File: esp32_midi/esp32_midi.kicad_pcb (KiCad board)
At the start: 2 copper layers, 2 parts, among them U1 ESP32-S3-WROOM-2, U2 AMS1117-3.3

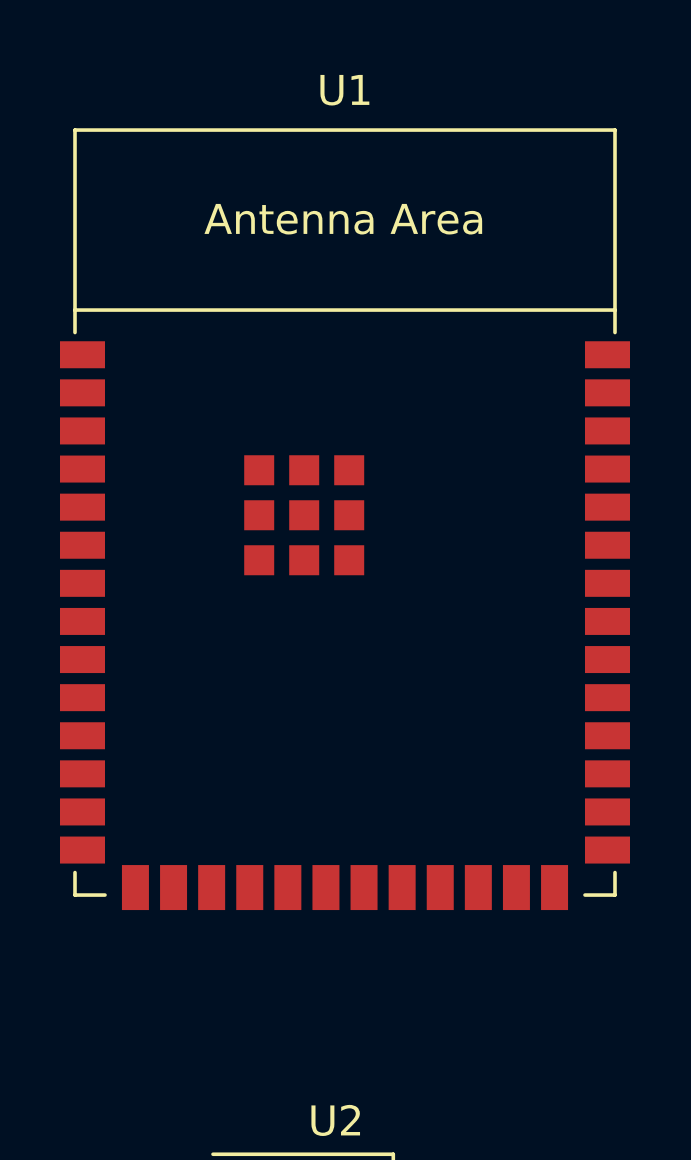
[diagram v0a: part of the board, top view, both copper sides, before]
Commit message: More footprints applied
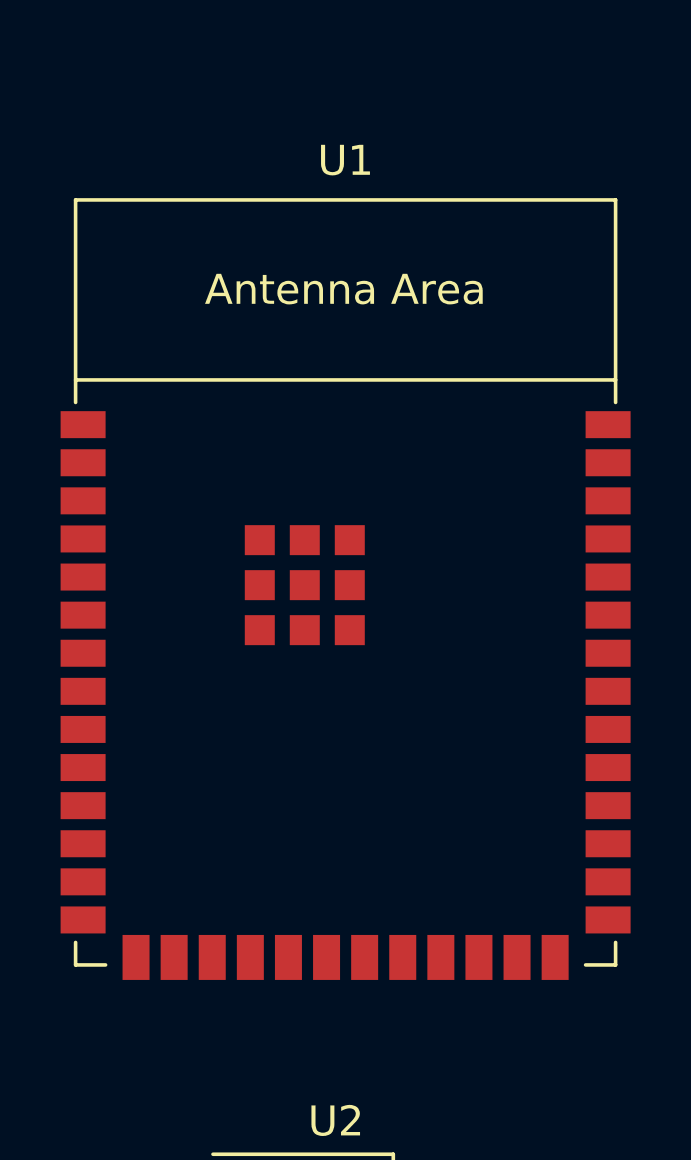
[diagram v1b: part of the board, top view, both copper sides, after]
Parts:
- moved U1 2.33 mm to (111.6, 50.1)

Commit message: Add ordentliche-teile
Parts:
- removed U1: ESP32-S3-WROOM-2, Espressif:ESP32-S3-WROOM-2
- removed U2: AMS1117-3.3, Package_TO_SOT_SMD:SOT-223-3_TabPin2

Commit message: Started work on PCB
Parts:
- added C1: 100n, Capacitor_SMD:C_0402_1005Metric, F.Cu at (380.5, 28.0)
- added C10: 10u, Capacitor_SMD:C_0603_1608Metric, F.Cu at (390.2, 109.4)
- added C2: 100n, Capacitor_SMD:C_0402_1005Metric, F.Cu at (380.5, 30.0)
- added C3: 100n, Capacitor_SMD:C_0402_1005Metric, F.Cu at (380.5, 31.9)
- added C4: 680µF, Capacitor_SMD:CP_Elec_10x10, F.Cu at (368.4, 69.8)
- added C5: 220µF, Capacitor_SMD:CP_Elec_10x10, F.Cu at (368.4, 81.7)
- added C6: 100n, Capacitor_SMD:C_0402_1005Metric, F.Cu at (380.5, 33.9)
- added C7: 100n, Capacitor_SMD:C_0402_1005Metric, F.Cu at (389.7, 111.6)
- added C8: 1u, Capacitor_SMD:C_0603_1608Metric, F.Cu at (390.2, 106.9)
- added C9: 100n, Capacitor_SMD:C_0402_1005Metric, F.Cu at (389.7, 113.6)
- added D1: D, Diode_SMD:D_SOD-123, F.Cu at (344.4, 14.4)
- added D10: WS2812B, LED_SMD:LED_WS2812B_PLCC4_5.0x5.0mm_P3.2mm, F.Cu at (185.6, 74.3)
- added D11: WS2812B, LED_SMD:LED_WS2812B_PLCC4_5.0x5.0mm_P3.2mm, F.Cu at (207.1, 74.3)
- added D12: WS2812B, LED_SMD:LED_WS2812B_PLCC4_5.0x5.0mm_P3.2mm, F.Cu at (228.6, 74.3)
- added D13: WS2812B, LED_SMD:LED_WS2812B_PLCC4_5.0x5.0mm_P3.2mm, F.Cu at (250.1, 74.3)
- added D14: WS2812B, LED_SMD:LED_WS2812B_PLCC4_5.0x5.0mm_P3.2mm, F.Cu at (271.6, 74.3)
- added D15: WS2812B, LED_SMD:LED_WS2812B_PLCC4_5.0x5.0mm_P3.2mm, F.Cu at (293.1, 74.3)
- added D16: WS2812B, LED_SMD:LED_WS2812B_PLCC4_5.0x5.0mm_P3.2mm, F.Cu at (314.6, 74.3)
- added D17: WS2812B, LED_SMD:LED_WS2812B_PLCC4_5.0x5.0mm_P3.2mm, F.Cu at (336.1, 74.3)
- added D18: WS2812B, LED_SMD:LED_WS2812B_PLCC4_5.0x5.0mm_P3.2mm, F.Cu at (185.6, 95.8)
- added D19: WS2812B, LED_SMD:LED_WS2812B_PLCC4_5.0x5.0mm_P3.2mm, F.Cu at (207.1, 95.8)
- added D2: D, Diode_SMD:D_SOD-123, F.Cu at (344.4, 17.8)
- added D20: WS2812B, LED_SMD:LED_WS2812B_PLCC4_5.0x5.0mm_P3.2mm, F.Cu at (228.6, 95.8)
- added D21: WS2812B, LED_SMD:LED_WS2812B_PLCC4_5.0x5.0mm_P3.2mm, F.Cu at (250.1, 95.8)
- added D22: WS2812B, LED_SMD:LED_WS2812B_PLCC4_5.0x5.0mm_P3.2mm, F.Cu at (271.6, 95.8)
- added D23: WS2812B, LED_SMD:LED_WS2812B_PLCC4_5.0x5.0mm_P3.2mm, F.Cu at (293.1, 95.8)
- added D24: WS2812B, LED_SMD:LED_WS2812B_PLCC4_5.0x5.0mm_P3.2mm, F.Cu at (314.6, 95.8)
- added D25: WS2812B, LED_SMD:LED_WS2812B_PLCC4_5.0x5.0mm_P3.2mm, F.Cu at (336.1, 95.8)
- added D26: WS2812B, LED_SMD:LED_WS2812B_PLCC4_5.0x5.0mm_P3.2mm, F.Cu at (185.6, 117.3)
- added D27: WS2812B, LED_SMD:LED_WS2812B_PLCC4_5.0x5.0mm_P3.2mm, F.Cu at (207.1, 117.3)
- added D28: WS2812B, LED_SMD:LED_WS2812B_PLCC4_5.0x5.0mm_P3.2mm, F.Cu at (228.6, 117.3)
- added D29: WS2812B, LED_SMD:LED_WS2812B_PLCC4_5.0x5.0mm_P3.2mm, F.Cu at (250.1, 117.3)
- added D3: D, Diode_SMD:D_SOD-123, F.Cu at (344.4, 21.1)
- added D30: WS2812B, LED_SMD:LED_WS2812B_PLCC4_5.0x5.0mm_P3.2mm, F.Cu at (271.6, 117.3)
- added D31: WS2812B, LED_SMD:LED_WS2812B_PLCC4_5.0x5.0mm_P3.2mm, F.Cu at (293.1, 117.3)
- added D32: WS2812B, LED_SMD:LED_WS2812B_PLCC4_5.0x5.0mm_P3.2mm, F.Cu at (314.6, 117.3)
- added D33: WS2812B, LED_SMD:LED_WS2812B_PLCC4_5.0x5.0mm_P3.2mm, F.Cu at (336.1, 117.3)
- added D34: WS2812B, LED_SMD:LED_WS2812B_PLCC4_5.0x5.0mm_P3.2mm, F.Cu at (185.6, 138.8)
- added D35: WS2812B, LED_SMD:LED_WS2812B_PLCC4_5.0x5.0mm_P3.2mm, F.Cu at (207.1, 138.8)
- added D36: WS2812B, LED_SMD:LED_WS2812B_PLCC4_5.0x5.0mm_P3.2mm, F.Cu at (228.6, 138.8)
- added D37: WS2812B, LED_SMD:LED_WS2812B_PLCC4_5.0x5.0mm_P3.2mm, F.Cu at (250.1, 138.8)
- added D38: WS2812B, LED_SMD:LED_WS2812B_PLCC4_5.0x5.0mm_P3.2mm, F.Cu at (271.6, 138.8)
- added D39: WS2812B, LED_SMD:LED_WS2812B_PLCC4_5.0x5.0mm_P3.2mm, F.Cu at (293.1, 138.8)
- added D4: D, Diode_SMD:D_SOD-123, F.Cu at (344.4, 24.5)
- added D40: WS2812B, LED_SMD:LED_WS2812B_PLCC4_5.0x5.0mm_P3.2mm, F.Cu at (314.6, 138.8)
- added D41: WS2812B, LED_SMD:LED_WS2812B_PLCC4_5.0x5.0mm_P3.2mm, F.Cu at (336.1, 138.8)
- added D42: WS2812B, LED_SMD:LED_WS2812B_PLCC4_5.0x5.0mm_P3.2mm, F.Cu at (185.6, 160.3)
- added D43: WS2812B, LED_SMD:LED_WS2812B_PLCC4_5.0x5.0mm_P3.2mm, F.Cu at (207.1, 160.3)
- added D44: WS2812B, LED_SMD:LED_WS2812B_PLCC4_5.0x5.0mm_P3.2mm, F.Cu at (228.6, 160.3)
- added D45: WS2812B, LED_SMD:LED_WS2812B_PLCC4_5.0x5.0mm_P3.2mm, F.Cu at (250.1, 160.3)
- added D46: WS2812B, LED_SMD:LED_WS2812B_PLCC4_5.0x5.0mm_P3.2mm, F.Cu at (271.6, 160.3)
- added D47: WS2812B, LED_SMD:LED_WS2812B_PLCC4_5.0x5.0mm_P3.2mm, F.Cu at (293.1, 160.3)
- added D48: WS2812B, LED_SMD:LED_WS2812B_PLCC4_5.0x5.0mm_P3.2mm, F.Cu at (314.6, 160.3)
- added D49: WS2812B, LED_SMD:LED_WS2812B_PLCC4_5.0x5.0mm_P3.2mm, F.Cu at (336.1, 160.3)
- added D5: 1N4148, Diode_SMD:D_SOD-123, F.Cu at (235.5, 38.5)
- added D50: WS2812B, LED_SMD:LED_WS2812B_PLCC4_5.0x5.0mm_P3.2mm, F.Cu at (185.6, 181.8)
- added D51: WS2812B, LED_SMD:LED_WS2812B_PLCC4_5.0x5.0mm_P3.2mm, F.Cu at (207.1, 181.8)
- added D52: WS2812B, LED_SMD:LED_WS2812B_PLCC4_5.0x5.0mm_P3.2mm, F.Cu at (228.6, 181.8)
- added D53: WS2812B, LED_SMD:LED_WS2812B_PLCC4_5.0x5.0mm_P3.2mm, F.Cu at (250.1, 181.8)
- added D54: WS2812B, LED_SMD:LED_WS2812B_PLCC4_5.0x5.0mm_P3.2mm, F.Cu at (271.6, 181.8)
- added D55: WS2812B, LED_SMD:LED_WS2812B_PLCC4_5.0x5.0mm_P3.2mm, F.Cu at (293.1, 181.8)
- added D56: WS2812B, LED_SMD:LED_WS2812B_PLCC4_5.0x5.0mm_P3.2mm, F.Cu at (314.6, 181.8)
- added D57: WS2812B, LED_SMD:LED_WS2812B_PLCC4_5.0x5.0mm_P3.2mm, F.Cu at (336.1, 181.8)
- added D58: WS2812B, LED_SMD:LED_WS2812B_PLCC4_5.0x5.0mm_P3.2mm, F.Cu at (185.6, 203.3)
- added D59: WS2812B, LED_SMD:LED_WS2812B_PLCC4_5.0x5.0mm_P3.2mm, F.Cu at (207.1, 203.3)
- added D6: LED, LED_SMD:LED_0603_1608Metric, F.Cu at (386.2, 106.9)
- added D60: WS2812B, LED_SMD:LED_WS2812B_PLCC4_5.0x5.0mm_P3.2mm, F.Cu at (228.6, 203.3)
- added D61: WS2812B, LED_SMD:LED_WS2812B_PLCC4_5.0x5.0mm_P3.2mm, F.Cu at (250.1, 203.3)
- added D62: WS2812B, LED_SMD:LED_WS2812B_PLCC4_5.0x5.0mm_P3.2mm, F.Cu at (271.6, 203.3)
- added D63: WS2812B, LED_SMD:LED_WS2812B_PLCC4_5.0x5.0mm_P3.2mm, F.Cu at (293.1, 203.3)
- added D64: WS2812B, LED_SMD:LED_WS2812B_PLCC4_5.0x5.0mm_P3.2mm, F.Cu at (314.6, 203.3)
- added D65: WS2812B, LED_SMD:LED_WS2812B_PLCC4_5.0x5.0mm_P3.2mm, F.Cu at (336.1, 203.3)
- added D66: WS2812B, LED_SMD:LED_WS2812B_PLCC4_5.0x5.0mm_P3.2mm, F.Cu at (185.6, 224.8)
- added D67: WS2812B, LED_SMD:LED_WS2812B_PLCC4_5.0x5.0mm_P3.2mm, F.Cu at (207.1, 224.8)
- added D68: WS2812B, LED_SMD:LED_WS2812B_PLCC4_5.0x5.0mm_P3.2mm, F.Cu at (228.6, 224.8)
- added D69: WS2812B, LED_SMD:LED_WS2812B_PLCC4_5.0x5.0mm_P3.2mm, F.Cu at (250.1, 224.8)
- added D7: LED, LED_SMD:LED_0603_1608Metric, F.Cu at (386.2, 109.5)
- added D70: WS2812B, LED_SMD:LED_WS2812B_PLCC4_5.0x5.0mm_P3.2mm, F.Cu at (271.6, 224.8)
- added D71: WS2812B, LED_SMD:LED_WS2812B_PLCC4_5.0x5.0mm_P3.2mm, F.Cu at (293.1, 224.8)
- added D72: WS2812B, LED_SMD:LED_WS2812B_PLCC4_5.0x5.0mm_P3.2mm, F.Cu at (314.6, 224.8)
- added D73: WS2812B, LED_SMD:LED_WS2812B_PLCC4_5.0x5.0mm_P3.2mm, F.Cu at (336.1, 224.8)
- added D74: WS2812B, LED_SMD:LED_WS2812B_PLCC4_5.0x5.0mm_P3.2mm, F.Cu at (185.6, 246.3)
- added D75: WS2812B, LED_SMD:LED_WS2812B_PLCC4_5.0x5.0mm_P3.2mm, F.Cu at (207.1, 246.3)
- added D76: WS2812B, LED_SMD:LED_WS2812B_PLCC4_5.0x5.0mm_P3.2mm, F.Cu at (228.6, 246.3)
- added D77: WS2812B, LED_SMD:LED_WS2812B_PLCC4_5.0x5.0mm_P3.2mm, F.Cu at (250.1, 246.3)
- added D78: WS2812B, LED_SMD:LED_WS2812B_PLCC4_5.0x5.0mm_P3.2mm, F.Cu at (271.6, 246.3)
- added D79: WS2812B, LED_SMD:LED_WS2812B_PLCC4_5.0x5.0mm_P3.2mm, F.Cu at (293.1, 246.3)
- added D8: LED, LED_SMD:LED_0603_1608Metric, F.Cu at (386.2, 112.1)
- added D80: WS2812B, LED_SMD:LED_WS2812B_PLCC4_5.0x5.0mm_P3.2mm, F.Cu at (314.6, 246.3)
- added D81: WS2812B, LED_SMD:LED_WS2812B_PLCC4_5.0x5.0mm_P3.2mm, F.Cu at (336.1, 246.3)
- added D82: SS54, Diode_SMD:D_SMA, F.Cu at (365.1, 89.9)
- added D9: LED5V, LED_SMD:LED_0603_1608Metric, F.Cu at (386.2, 114.7)
- added J1: Conn_Display, Connector_PinHeader_2.54mm:PinHeader_1x08_P2.54mm_Vertical, F.Cu at (222.5, 59.0)
- added J2: 5V-12V, Connector_BarrelJack:BarrelJack_Wuerth_6941xx301002, F.Cu at (307.6, 25.4)
- added J4: MIDI 1 OUT, ordentliche-teile:scheißmidi, F.Cu at (260.8, 11.5)
- added J5: MIDI 1 IN, ordentliche-teile:scheißmidi, F.Cu at (238.1, 11.7)
- added J6: MIDI 1 OUT, ordentliche-teile:scheißmidi, F.Cu at (215.0, 11.5)
- added L1: 33µH, Inductor_SMD:L_10.4x10.4_H4.8, F.Cu at (381.4, 82.2)
- added Q1: BSS138, Package_TO_SOT_SMD:SOT-23, F.Cu at (264.0, 32.0)
- added Q2: SS8050_C2150, Package_TO_SOT_SMD:TSOT-23, F.Cu at (401.1, 96.4)
- added Q3: SS8050_C2150, Package_TO_SOT_SMD:TSOT-23, F.Cu at (401.1, 100.8)
- added Q4: BSS138, Package_TO_SOT_SMD:SOT-23, F.Cu at (218.5, 30.6)
- added R1: 10k, Resistor_SMD:R_0402_1005Metric, F.Cu at (380.5, 35.9)
- added R10: 10k, Resistor_SMD:R_0402_1005Metric, F.Cu at (397.0, 95.2)
- added R11: 1k, Resistor_SMD:R_0402_1005Metric, F.Cu at (397.0, 97.1)
- added R12: 1k, Resistor_SMD:R_0402_1005Metric, F.Cu at (397.0, 99.1)
- added R13: 1k, Resistor_SMD:R_0402_1005Metric, F.Cu at (397.0, 101.1)
- added R14: 1k, Resistor_SMD:R_0402_1005Metric, F.Cu at (397.0, 103.1)
- added R15: 220, Resistor_SMD:R_0402_1005Metric, F.Cu at (210.0, 31.0)
- added R16: R_Variable, ordentliche-teile:scheißfader, B.Cu at (185.4, 324.0)
- added R17: R_Variable, ordentliche-teile:scheißfader, B.Cu at (206.9, 324.0)
- added R18: R_Variable, ordentliche-teile:scheißfader, B.Cu at (228.4, 324.0)
- added R19: R_Variable, ordentliche-teile:scheißfader, B.Cu at (249.9, 324.0)
- added R2: 220, Resistor_SMD:R_0402_1005Metric, F.Cu at (256.0, 30.0)
- added R20: R_Variable, ordentliche-teile:scheißfader, B.Cu at (271.4, 324.0)
- added R21: R_Variable, ordentliche-teile:scheißfader, B.Cu at (292.9, 324.0)
- added R22: R_Variable, ordentliche-teile:scheißfader, B.Cu at (314.4, 324.0)
- added R23: R_Variable, ordentliche-teile:scheißfader, B.Cu at (335.9, 324.0)
- added R24: R_Variable, Potentiometer_THT:Potentiometer_Alps_RK09L_Single_Vertical, F.Cu at (184.5, 262.5)
- added R25: R_Variable, Potentiometer_THT:Potentiometer_Alps_RK09L_Single_Vertical, F.Cu at (206.0, 262.5)
- added R26: R_Variable, Potentiometer_THT:Potentiometer_Alps_RK09L_Single_Vertical, F.Cu at (227.5, 262.5)
- added R27: R_Variable, Potentiometer_THT:Potentiometer_Alps_RK09L_Single_Vertical, F.Cu at (249.0, 262.5)
- added R28: R_Variable, Potentiometer_THT:Potentiometer_Alps_RK09L_Single_Vertical, F.Cu at (270.5, 262.5)
- added R29: R_Variable, Potentiometer_THT:Potentiometer_Alps_RK09L_Single_Vertical, F.Cu at (292.0, 262.5)
- added R3: 220, Resistor_SMD:R_0402_1005Metric, F.Cu at (241.0, 44.5)
- added R30: R_Variable, Potentiometer_THT:Potentiometer_Alps_RK09L_Single_Vertical, F.Cu at (313.5, 262.5)
- added R31: R_Variable, Potentiometer_THT:Potentiometer_Alps_RK09L_Single_Vertical, F.Cu at (335.0, 262.5)
- added R32: R_Variable, Potentiometer_THT:Potentiometer_Alps_RK09L_Single_Vertical, F.Cu at (184.5, 284.0)
- added R33: R_Variable, Potentiometer_THT:Potentiometer_Alps_RK09L_Single_Vertical, F.Cu at (206.0, 284.0)
- added R34: R_Variable, Potentiometer_THT:Potentiometer_Alps_RK09L_Single_Vertical, F.Cu at (227.5, 284.0)
- added R35: R_Variable, Potentiometer_THT:Potentiometer_Alps_RK09L_Single_Vertical, F.Cu at (249.0, 284.0)
- added R36: R_Variable, Potentiometer_THT:Potentiometer_Alps_RK09L_Single_Vertical, F.Cu at (270.5, 284.0)
- added R37: R_Variable, Potentiometer_THT:Potentiometer_Alps_RK09L_Single_Vertical, F.Cu at (292.0, 284.0)
- added R38: R_Variable, Potentiometer_THT:Potentiometer_Alps_RK09L_Single_Vertical, F.Cu at (313.5, 284.0)
- added R39: R_Variable, Potentiometer_THT:Potentiometer_Alps_RK09L_Single_Vertical, F.Cu at (335.0, 284.0)
- added R4: 220, Resistor_SMD:R_0402_1005Metric, F.Cu at (233.0, 33.0)
- added R40: R_Variable, Potentiometer_THT:Potentiometer_Alps_RK09L_Single_Vertical, F.Cu at (184.5, 305.5)
- added R41: R_Variable, Potentiometer_THT:Potentiometer_Alps_RK09L_Single_Vertical, F.Cu at (206.0, 305.5)
- added R42: R_Variable, Potentiometer_THT:Potentiometer_Alps_RK09L_Single_Vertical, F.Cu at (227.5, 305.5)
- added R43: R_Variable, Potentiometer_THT:Potentiometer_Alps_RK09L_Single_Vertical, F.Cu at (249.0, 305.5)
- added R44: R_Variable, Potentiometer_THT:Potentiometer_Alps_RK09L_Single_Vertical, F.Cu at (270.5, 305.5)
- added R45: R_Variable, Potentiometer_THT:Potentiometer_Alps_RK09L_Single_Vertical, F.Cu at (292.0, 305.5)
- added R46: R_Variable, Potentiometer_THT:Potentiometer_Alps_RK09L_Single_Vertical, F.Cu at (313.5, 305.5)
- added R47: R_Variable, Potentiometer_THT:Potentiometer_Alps_RK09L_Single_Vertical, F.Cu at (335.0, 305.5)
- added R48: 10k, Resistor_SMD:R_0402_1005Metric, F.Cu at (472.0, 175.0)
- added R49: 10k, Resistor_SMD:R_0402_1005Metric, F.Cu at (472.5, 180.5)
- added R5: 12k, Resistor_SMD:R_0402_1005Metric, F.Cu at (394.1, 95.2)
- added R50: 10k, Resistor_SMD:R_0402_1005Metric, F.Cu at (479.1, 194.9)
- added R51: 5k1, Resistor_SMD:R_0402_1005Metric, F.Cu at (380.5, 37.9)
- added R52: 5k1, Resistor_SMD:R_0402_1005Metric, F.Cu at (380.5, 39.9)
- added R6: 12k, Resistor_SMD:R_0402_1005Metric, F.Cu at (394.1, 97.1)
- added R7: 5k1, Resistor_SMD:R_0402_1005Metric, F.Cu at (394.1, 99.1)
- added R8: 5k1, Resistor_SMD:R_0402_1005Metric, F.Cu at (394.1, 101.1)
- added R9: 10k, Resistor_SMD:R_0402_1005Metric, F.Cu at (394.1, 103.1)
- added SW1: SW_SPST, Button_Switch_THT:SW_PUSH_6mm_H13mm, F.Cu at (179.8, 22.2)
- added SW10: SW_SPST, ordentliche-teile:scheißbutton, F.Cu at (178.5, 102.0)
- added SW11: SW_SPST, ordentliche-teile:scheißbutton, F.Cu at (200.0, 102.0)
- added SW12: SW_SPST, ordentliche-teile:scheißbutton, F.Cu at (221.5, 102.0)
- added SW13: SW_SPST, ordentliche-teile:scheißbutton, F.Cu at (243.0, 102.0)
- added SW14: SW_SPST, ordentliche-teile:scheißbutton, F.Cu at (264.5, 102.0)
- added SW15: SW_SPST, ordentliche-teile:scheißbutton, F.Cu at (286.0, 102.0)
- added SW16: SW_SPST, ordentliche-teile:scheißbutton, F.Cu at (307.5, 102.0)
- added SW17: SW_SPST, ordentliche-teile:scheißbutton, F.Cu at (329.0, 102.0)
- added SW18: SW_SPST, ordentliche-teile:scheißbutton, F.Cu at (178.5, 123.5)
- added SW19: SW_SPST, ordentliche-teile:scheißbutton, F.Cu at (200.0, 123.5)
- added SW2: SW_SPST, ordentliche-teile:scheißbutton, F.Cu at (178.5, 80.5)
- added SW20: SW_SPST, ordentliche-teile:scheißbutton, F.Cu at (221.5, 123.5)
- added SW21: SW_SPST, ordentliche-teile:scheißbutton, F.Cu at (243.0, 123.5)
- added SW22: SW_SPST, ordentliche-teile:scheißbutton, F.Cu at (264.5, 123.5)
- added SW23: SW_SPST, ordentliche-teile:scheißbutton, F.Cu at (286.0, 123.5)
- added SW24: SW_SPST, ordentliche-teile:scheißbutton, F.Cu at (307.5, 123.5)
- added SW25: SW_SPST, ordentliche-teile:scheißbutton, F.Cu at (329.0, 123.5)
- added SW26: SW_SPST, ordentliche-teile:scheißbutton, F.Cu at (178.5, 145.0)
- added SW27: SW_SPST, ordentliche-teile:scheißbutton, F.Cu at (200.0, 145.0)
- added SW28: SW_SPST, ordentliche-teile:scheißbutton, F.Cu at (221.5, 145.0)
- added SW29: SW_SPST, ordentliche-teile:scheißbutton, F.Cu at (243.0, 145.0)
- added SW3: SW_SPST, ordentliche-teile:scheißbutton, F.Cu at (200.0, 80.5)
- added SW30: SW_SPST, ordentliche-teile:scheißbutton, F.Cu at (264.5, 145.0)
- added SW31: SW_SPST, ordentliche-teile:scheißbutton, F.Cu at (286.0, 145.0)
- added SW32: SW_SPST, ordentliche-teile:scheißbutton, F.Cu at (307.5, 145.0)
- added SW33: SW_SPST, ordentliche-teile:scheißbutton, F.Cu at (329.0, 145.0)
- added SW34: SW_SPST, ordentliche-teile:scheißbutton, F.Cu at (178.5, 166.5)
- added SW35: SW_SPST, ordentliche-teile:scheißbutton, F.Cu at (200.0, 166.5)
- added SW36: SW_SPST, ordentliche-teile:scheißbutton, F.Cu at (221.5, 166.5)
- added SW37: SW_SPST, ordentliche-teile:scheißbutton, F.Cu at (243.0, 166.5)
- added SW38: SW_SPST, ordentliche-teile:scheißbutton, F.Cu at (264.5, 166.5)
- added SW39: SW_SPST, ordentliche-teile:scheißbutton, F.Cu at (286.0, 166.5)
- added SW4: SW_SPST, ordentliche-teile:scheißbutton, F.Cu at (221.5, 80.5)
- added SW40: SW_SPST, ordentliche-teile:scheißbutton, F.Cu at (307.5, 166.5)
- added SW41: SW_SPST, ordentliche-teile:scheißbutton, F.Cu at (329.0, 166.5)
- added SW42: SW_SPST, ordentliche-teile:scheißbutton, F.Cu at (178.5, 188.0)
- added SW43: SW_SPST, ordentliche-teile:scheißbutton, F.Cu at (200.0, 188.0)
- added SW44: SW_SPST, ordentliche-teile:scheißbutton, F.Cu at (221.5, 188.0)
- added SW45: SW_SPST, ordentliche-teile:scheißbutton, F.Cu at (243.0, 188.0)
- added SW46: SW_SPST, ordentliche-teile:scheißbutton, F.Cu at (264.5, 188.0)
- added SW47: SW_SPST, ordentliche-teile:scheißbutton, F.Cu at (286.0, 188.0)
- added SW48: SW_SPST, ordentliche-teile:scheißbutton, F.Cu at (307.5, 188.0)
- added SW49: SW_SPST, ordentliche-teile:scheißbutton, F.Cu at (329.0, 188.0)
- added SW5: SW_SPST, ordentliche-teile:scheißbutton, F.Cu at (243.0, 80.5)
- added SW50: SW_SPST, ordentliche-teile:scheißbutton, F.Cu at (178.5, 209.5)
- added SW51: SW_SPST, ordentliche-teile:scheißbutton, F.Cu at (200.0, 209.5)
- added SW52: SW_SPST, ordentliche-teile:scheißbutton, F.Cu at (221.5, 209.5)
- added SW53: SW_SPST, ordentliche-teile:scheißbutton, F.Cu at (243.0, 209.5)
- added SW54: SW_SPST, ordentliche-teile:scheißbutton, F.Cu at (264.5, 209.5)
- added SW55: SW_SPST, ordentliche-teile:scheißbutton, F.Cu at (286.0, 209.5)
- added SW56: SW_SPST, ordentliche-teile:scheißbutton, F.Cu at (307.5, 209.5)
- added SW57: SW_SPST, ordentliche-teile:scheißbutton, F.Cu at (329.0, 209.5)
- added SW58: SW_SPST, ordentliche-teile:scheißbutton, F.Cu at (178.5, 231.0)
- added SW59: SW_SPST, ordentliche-teile:scheißbutton, F.Cu at (200.0, 231.0)
- added SW6: SW_SPST, ordentliche-teile:scheißbutton, F.Cu at (264.5, 80.5)
- added SW60: SW_SPST, ordentliche-teile:scheißbutton, F.Cu at (221.5, 231.0)
- added SW61: SW_SPST, ordentliche-teile:scheißbutton, F.Cu at (243.0, 231.0)
- added SW62: SW_SPST, ordentliche-teile:scheißbutton, F.Cu at (264.5, 231.0)
- added SW63: SW_SPST, ordentliche-teile:scheißbutton, F.Cu at (286.0, 231.0)
- added SW64: SW_SPST, ordentliche-teile:scheißbutton, F.Cu at (307.5, 231.0)
- added SW65: SW_SPST, ordentliche-teile:scheißbutton, F.Cu at (329.0, 231.0)
- added SW66: SW_SPST, ordentliche-teile:scheißbutton, F.Cu at (178.5, 252.5)
- added SW67: SW_SPST, ordentliche-teile:scheißbutton, F.Cu at (200.0, 252.5)
- added SW68: SW_SPST, ordentliche-teile:scheißbutton, F.Cu at (221.5, 252.5)
- added SW69: SW_SPST, ordentliche-teile:scheißbutton, F.Cu at (243.0, 252.5)
- added SW7: SW_SPST, ordentliche-teile:scheißbutton, F.Cu at (286.0, 80.5)
- added SW70: SW_SPST, ordentliche-teile:scheißbutton, F.Cu at (264.5, 252.5)
- added SW71: SW_SPST, ordentliche-teile:scheißbutton, F.Cu at (286.0, 252.5)
- added SW72: SW_SPST, ordentliche-teile:scheißbutton, F.Cu at (307.5, 252.5)
- added SW73: SW_SPST, ordentliche-teile:scheißbutton, F.Cu at (329.0, 252.5)
- added SW74: SW_SPST, ordentliche-teile:bobbybutton, F.Cu at (284.9, 40.3)
- added SW75: SW_SPST, ordentliche-teile:bobbybutton, F.Cu at (284.9, 45.5)
- added SW76: SW_SPST, ordentliche-teile:bobbybutton, F.Cu at (284.9, 50.7)
- added SW77: SW_SPST, ordentliche-teile:bobbybutton, F.Cu at (284.9, 55.9)
- added SW78: SW_SPST, Connector_PinSocket_2.54mm:PinSocket_1x02_P2.54mm_Vertical, F.Cu at (280.5, 16.5)
- added SW79: SW_SPST, Connector_PinSocket_2.54mm:PinSocket_1x02_P2.54mm_Vertical, F.Cu at (285.1, 16.5)
- added SW8: SW_SPST, ordentliche-teile:scheißbutton, F.Cu at (307.5, 80.5)
- added SW80: SW_SPST, Connector_PinSocket_2.54mm:PinSocket_1x02_P2.54mm_Vertical, F.Cu at (289.7, 16.5)
- added SW81: SW_SPST, Connector_PinSocket_2.54mm:PinSocket_1x02_P2.54mm_Vertical, F.Cu at (294.3, 16.5)
- added SW9: SW_SPST, ordentliche-teile:scheißbutton, F.Cu at (329.0, 80.5)
- added U1: ESP32-S3-WROOM-2, Espressif:ESP32-S3-WROOM-2, F.Cu at (263.2, 53.4)
- added U10: BL1551, Package_TO_SOT_SMD:SOT-363_SC-70-6, F.Cu at (279.1, 341.4)
- added U100: BL1551, Package_TO_SOT_SMD:SOT-363_SC-70-6, F.Cu at (445.0, 196.2)
- added U101: BL1551, Package_TO_SOT_SMD:SOT-363_SC-70-6, F.Cu at (447.0, 202.2)
- added U102: USBLC6-4SC6, Package_TO_SOT_SMD:SOT-23-6, F.Cu at (444.2, 246.1)
- added U103: BL1551, Package_TO_SOT_SMD:SOT-363_SC-70-6, F.Cu at (446.6, 208.8)
- added U104: BL1551, Package_TO_SOT_SMD:SOT-363_SC-70-6, F.Cu at (469.5, 229.2)
- added U105: BL1551, Package_TO_SOT_SMD:SOT-363_SC-70-6, F.Cu at (436.5, 138.4)
- added U106: BL1551, Package_TO_SOT_SMD:SOT-363_SC-70-6, F.Cu at (442.6, 148.4)
- added U107: USBLC6-4SC6, Package_TO_SOT_SMD:SOT-23-6, F.Cu at (402.0, 227.0)
- added U108: BL1551, Package_TO_SOT_SMD:SOT-363_SC-70-6, F.Cu at (482.4, 243.8)
- added U109: BL1551, Package_TO_SOT_SMD:SOT-363_SC-70-6, F.Cu at (447.5, 161.6)
- added U11: BL1551, Package_TO_SOT_SMD:SOT-363_SC-70-6, F.Cu at (299.4, 330.4)
- added U110: BL1551, Package_TO_SOT_SMD:SOT-363_SC-70-6, F.Cu at (452.1, 175.6)
- added U111: BL1551, Package_TO_SOT_SMD:SOT-363_SC-70-6, F.Cu at (452.6, 182.9)
- added U112: USBLC6-4SC6, Package_TO_SOT_SMD:SOT-23-6, F.Cu at (377.4, 194.8)
- added U113: BL1551, Package_TO_SOT_SMD:SOT-363_SC-70-6, F.Cu at (452.8, 189.8)
- added U114: BL1551, Package_TO_SOT_SMD:SOT-363_SC-70-6, F.Cu at (374.9, 309.3)
- added U115: BL1551, Package_TO_SOT_SMD:SOT-363_SC-70-6, F.Cu at (454.0, 197.2)
- added U116: BL1551, Package_TO_SOT_SMD:SOT-363_SC-70-6, F.Cu at (456.0, 203.2)
- added U117: USBLC6-4SC6, Package_TO_SOT_SMD:SOT-23-6, F.Cu at (463.0, 246.2)
- added U118: BL1551, Package_TO_SOT_SMD:SOT-363_SC-70-6, F.Cu at (455.6, 209.8)
- added U119: BL1551, Package_TO_SOT_SMD:SOT-363_SC-70-6, F.Cu at (455.3, 218.1)
- added U12: BL1551, Package_TO_SOT_SMD:SOT-363_SC-70-6, F.Cu at (321.4, 341.4)
- added U120: BL1551, Package_TO_SOT_SMD:SOT-363_SC-70-6, F.Cu at (471.5, 196.6)
- added U121: BL1551, Package_TO_SOT_SMD:SOT-363_SC-70-6, F.Cu at (442.9, 138.3)
- added U122: USBLC6-4SC6, Package_TO_SOT_SMD:SOT-23-6, F.Cu at (477.7, 211.2)
- added U123: BL1551, Package_TO_SOT_SMD:SOT-363_SC-70-6, F.Cu at (449.2, 148.6)
- added U124: BL1551, Package_TO_SOT_SMD:SOT-363_SC-70-6, F.Cu at (454.5, 162.8)
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
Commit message: More PCB implementations
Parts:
- moved U132 294.5 mm to (288.1, 28.6)
- moved U133 288.3 mm to (294.1, 25.1)
- moved U130 281.7 mm to (282.1, 25.1)
- moved U115 269.0 mm to (188.6, 240.8)
- moved U105 260.4 mm to (189.0, 219.5)
- moved U117 254.6 mm to (208.6, 235.9)
- moved U95 254.3 mm to (188.5, 198.0)
- moved U108 251.6 mm to (232.0, 219.5)
- moved U85 246.4 mm to (189.6, 176.3)
- moved U116 243.9 mm to (214.3, 235.9)
- moved U104 243.4 mm to (279.5, 77.0)
- moved R50 243.4 mm to (271.5, 68.0), turned to 90 degrees
- moved U43 241.0 mm to (198.5, 58.5)
- moved U106 238.3 mm to (213.6, 214.4)
- moved U36 238.2 mm to (185.5, 45.5)
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
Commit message: More pcb
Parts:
- added H1: MountingHole_Pad, MountingHole:MountingHole_4mm_Pad_Via, F.Cu at (176.2, 16.6)
- added H2: MountingHole_Pad, MountingHole:MountingHole_4mm_Pad_Via, F.Cu at (339.2, 16.5)
- added H3: MountingHole_Pad, MountingHole:MountingHole_4mm_Pad_Via, F.Cu at (192.7, 399.6)
- added H4: MountingHole_Pad, MountingHole:MountingHole_4mm_Pad_Via, F.Cu at (321.9, 398.7)
- C1, C2, C3, C6: footprint Capacitor_SMD:C_0402_1005Metric -> Capacitor_SMD:C_1206_3216Metric
- R1, R10, R11, R12, R13, R14, R15, R2, R3, R4, R48, R49, R5, R50, R51, R52, R6, R7, R8, R9: footprint Resistor_SMD:R_0402_1005Metric -> Resistor_SMD:R_1206_3216Metric
- R16, R17, R18, R19, R20, R21, R22, R23: moved to F.Cu
- moved R1 168.6 mm to (199.1, 32.2), turned to 180 degrees
- moved D3 158.6 mm to (193.2, 24.8), turned to 90 degrees
- moved C2 123.4 mm to (247.7, 72.6), turned to -90 degrees
- moved C1 112.3 mm to (254.8, 43.8), turned to 90 degrees
- moved L1 77.9 mm to (286.2, 51.9)
- moved R9 74.7 mm to (314.9, 30.8)
- moved C4 68.3 mm to (283.9, 37.2), turned to 90 degrees
- moved R6 67.5 mm to (314.9, 33.6)
- moved R10 65.6 mm to (314.9, 36.4)
- moved C5 62.0 mm to (297.4, 36.2), turned to 90 degrees
- moved R5 61.6 mm to (314.9, 39.2), turned to 180 degrees
- moved D82 59.9 mm to (287.1, 65.2), turned to -90 degrees
- moved U2 59.5 mm to (306.9, 52.3)
- moved D2 46.2 mm to (307.1, 41.4)
- moved D1 38.8 mm to (317.0, 43.0), turned to 180 degrees
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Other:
- board outline added: 172 x 392.2 mm

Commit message: improve component spacing, add more LEDs
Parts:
- removed D10, D11, D12, D13, D14, D15, D16, D17, D18, D19, D20, D21, D22, D23, D24, D25, D26, D27, D28, D29, D30, D31, D32, D33, D34, D35, D36, D37, D38, D39, D40, D41, D42, D43, D44, D45, D46, D47, D48, D49, D50, D51, D52, D53, D54, D55, D56, D57, D58, D59, D60, D61, D62, D63, D64, D65, D66, D67, D68, D69, D70, D71, D72, D73, D74, D75, D76, D77, D78, D79, D80, D81: WS2812B, LED_SMD:LED_WS2812B_PLCC4_5.0x5.0mm_P3.2mm
- added D101: WS2812B, LED_SMD:LED_WS2812B_PLCC4_5.0x5.0mm_P3.2mm, F.Cu at (176.0, 95.0)
- added D102: WS2812B, LED_SMD:LED_WS2812B_PLCC4_5.0x5.0mm_P3.2mm, F.Cu at (188.0, 95.0)
- added D103: WS2812B, LED_SMD:LED_WS2812B_PLCC4_5.0x5.0mm_P3.2mm, F.Cu at (197.5, 95.0)
- added D104: WS2812B, LED_SMD:LED_WS2812B_PLCC4_5.0x5.0mm_P3.2mm, F.Cu at (209.5, 95.0)
- added D105: WS2812B, LED_SMD:LED_WS2812B_PLCC4_5.0x5.0mm_P3.2mm, F.Cu at (219.0, 95.0)
- added D106: WS2812B, LED_SMD:LED_WS2812B_PLCC4_5.0x5.0mm_P3.2mm, F.Cu at (231.0, 95.0)
- added D107: WS2812B, LED_SMD:LED_WS2812B_PLCC4_5.0x5.0mm_P3.2mm, F.Cu at (240.5, 95.0)
- added D108: WS2812B, LED_SMD:LED_WS2812B_PLCC4_5.0x5.0mm_P3.2mm, F.Cu at (252.5, 95.0)
- added D109: WS2812B, LED_SMD:LED_WS2812B_PLCC4_5.0x5.0mm_P3.2mm, F.Cu at (262.0, 95.0)
- added D110: WS2812B, LED_SMD:LED_WS2812B_PLCC4_5.0x5.0mm_P3.2mm, F.Cu at (274.0, 95.0)
- added D111: WS2812B, LED_SMD:LED_WS2812B_PLCC4_5.0x5.0mm_P3.2mm, F.Cu at (283.5, 95.0)
- added D112: WS2812B, LED_SMD:LED_WS2812B_PLCC4_5.0x5.0mm_P3.2mm, F.Cu at (295.5, 95.0)
- added D113: WS2812B, LED_SMD:LED_WS2812B_PLCC4_5.0x5.0mm_P3.2mm, F.Cu at (305.0, 95.0)
- added D114: WS2812B, LED_SMD:LED_WS2812B_PLCC4_5.0x5.0mm_P3.2mm, F.Cu at (317.0, 95.0)
- added D115: WS2812B, LED_SMD:LED_WS2812B_PLCC4_5.0x5.0mm_P3.2mm, F.Cu at (326.5, 95.0)
- added D116: WS2812B, LED_SMD:LED_WS2812B_PLCC4_5.0x5.0mm_P3.2mm, F.Cu at (338.5, 95.0)
- added D117: WS2812B, LED_SMD:LED_WS2812B_PLCC4_5.0x5.0mm_P3.2mm, F.Cu at (176.0, 116.5)
- added D118: WS2812B, LED_SMD:LED_WS2812B_PLCC4_5.0x5.0mm_P3.2mm, F.Cu at (188.0, 116.5)
- added D119: WS2812B, LED_SMD:LED_WS2812B_PLCC4_5.0x5.0mm_P3.2mm, F.Cu at (197.5, 116.5)
- added D120: WS2812B, LED_SMD:LED_WS2812B_PLCC4_5.0x5.0mm_P3.2mm, F.Cu at (209.5, 116.5)
- added D121: WS2812B, LED_SMD:LED_WS2812B_PLCC4_5.0x5.0mm_P3.2mm, F.Cu at (219.0, 116.5)
- added D122: WS2812B, LED_SMD:LED_WS2812B_PLCC4_5.0x5.0mm_P3.2mm, F.Cu at (231.0, 116.5)
- added D123: WS2812B, LED_SMD:LED_WS2812B_PLCC4_5.0x5.0mm_P3.2mm, F.Cu at (240.5, 116.5)
- added D124: WS2812B, LED_SMD:LED_WS2812B_PLCC4_5.0x5.0mm_P3.2mm, F.Cu at (252.5, 116.5)
- added D125: WS2812B, LED_SMD:LED_WS2812B_PLCC4_5.0x5.0mm_P3.2mm, F.Cu at (262.0, 116.5)
- added D126: WS2812B, LED_SMD:LED_WS2812B_PLCC4_5.0x5.0mm_P3.2mm, F.Cu at (274.0, 116.5)
- added D127: WS2812B, LED_SMD:LED_WS2812B_PLCC4_5.0x5.0mm_P3.2mm, F.Cu at (283.5, 116.5)
- added D128: WS2812B, LED_SMD:LED_WS2812B_PLCC4_5.0x5.0mm_P3.2mm, F.Cu at (295.5, 116.5)
- added D129: WS2812B, LED_SMD:LED_WS2812B_PLCC4_5.0x5.0mm_P3.2mm, F.Cu at (305.0, 116.5)
- added D130: WS2812B, LED_SMD:LED_WS2812B_PLCC4_5.0x5.0mm_P3.2mm, F.Cu at (317.0, 116.5)
- added D131: WS2812B, LED_SMD:LED_WS2812B_PLCC4_5.0x5.0mm_P3.2mm, F.Cu at (326.5, 116.5)
- added D132: WS2812B, LED_SMD:LED_WS2812B_PLCC4_5.0x5.0mm_P3.2mm, F.Cu at (338.5, 116.5)
- added D133: WS2812B, LED_SMD:LED_WS2812B_PLCC4_5.0x5.0mm_P3.2mm, F.Cu at (176.0, 138.0)
- added D134: WS2812B, LED_SMD:LED_WS2812B_PLCC4_5.0x5.0mm_P3.2mm, F.Cu at (188.0, 138.0)
- added D135: WS2812B, LED_SMD:LED_WS2812B_PLCC4_5.0x5.0mm_P3.2mm, F.Cu at (197.5, 138.0)
- added D136: WS2812B, LED_SMD:LED_WS2812B_PLCC4_5.0x5.0mm_P3.2mm, F.Cu at (209.5, 138.0)
- added D137: WS2812B, LED_SMD:LED_WS2812B_PLCC4_5.0x5.0mm_P3.2mm, F.Cu at (219.0, 138.0)
- added D138: WS2812B, LED_SMD:LED_WS2812B_PLCC4_5.0x5.0mm_P3.2mm, F.Cu at (231.0, 138.0)
- added D139: WS2812B, LED_SMD:LED_WS2812B_PLCC4_5.0x5.0mm_P3.2mm, F.Cu at (240.5, 138.0)
- added D140: WS2812B, LED_SMD:LED_WS2812B_PLCC4_5.0x5.0mm_P3.2mm, F.Cu at (252.5, 138.0)
- added D141: WS2812B, LED_SMD:LED_WS2812B_PLCC4_5.0x5.0mm_P3.2mm, F.Cu at (262.0, 138.0)
- added D142: WS2812B, LED_SMD:LED_WS2812B_PLCC4_5.0x5.0mm_P3.2mm, F.Cu at (274.0, 138.0)
- added D143: WS2812B, LED_SMD:LED_WS2812B_PLCC4_5.0x5.0mm_P3.2mm, F.Cu at (283.5, 138.0)
- added D144: WS2812B, LED_SMD:LED_WS2812B_PLCC4_5.0x5.0mm_P3.2mm, F.Cu at (295.5, 138.0)
- added D145: WS2812B, LED_SMD:LED_WS2812B_PLCC4_5.0x5.0mm_P3.2mm, F.Cu at (305.0, 138.0)
- added D146: WS2812B, LED_SMD:LED_WS2812B_PLCC4_5.0x5.0mm_P3.2mm, F.Cu at (317.0, 138.0)
- added D147: WS2812B, LED_SMD:LED_WS2812B_PLCC4_5.0x5.0mm_P3.2mm, F.Cu at (326.5, 138.0)
- added D148: WS2812B, LED_SMD:LED_WS2812B_PLCC4_5.0x5.0mm_P3.2mm, F.Cu at (338.5, 138.0)
- added D149: WS2812B, LED_SMD:LED_WS2812B_PLCC4_5.0x5.0mm_P3.2mm, F.Cu at (176.0, 159.5)
- added D150: WS2812B, LED_SMD:LED_WS2812B_PLCC4_5.0x5.0mm_P3.2mm, F.Cu at (188.0, 159.5)
- added D151: WS2812B, LED_SMD:LED_WS2812B_PLCC4_5.0x5.0mm_P3.2mm, F.Cu at (197.5, 159.5)
- added D152: WS2812B, LED_SMD:LED_WS2812B_PLCC4_5.0x5.0mm_P3.2mm, F.Cu at (209.5, 159.5)
- added D153: WS2812B, LED_SMD:LED_WS2812B_PLCC4_5.0x5.0mm_P3.2mm, F.Cu at (219.0, 159.5)
- added D154: WS2812B, LED_SMD:LED_WS2812B_PLCC4_5.0x5.0mm_P3.2mm, F.Cu at (231.0, 159.5)
- added D155: WS2812B, LED_SMD:LED_WS2812B_PLCC4_5.0x5.0mm_P3.2mm, F.Cu at (240.5, 159.5)
- added D156: WS2812B, LED_SMD:LED_WS2812B_PLCC4_5.0x5.0mm_P3.2mm, F.Cu at (252.5, 159.5)
- added D157: WS2812B, LED_SMD:LED_WS2812B_PLCC4_5.0x5.0mm_P3.2mm, F.Cu at (262.0, 159.5)
- added D158: WS2812B, LED_SMD:LED_WS2812B_PLCC4_5.0x5.0mm_P3.2mm, F.Cu at (274.0, 159.5)
- added D159: WS2812B, LED_SMD:LED_WS2812B_PLCC4_5.0x5.0mm_P3.2mm, F.Cu at (283.5, 159.5)
- added D160: WS2812B, LED_SMD:LED_WS2812B_PLCC4_5.0x5.0mm_P3.2mm, F.Cu at (295.5, 159.5)
- added D161: WS2812B, LED_SMD:LED_WS2812B_PLCC4_5.0x5.0mm_P3.2mm, F.Cu at (305.0, 159.5)
- added D162: WS2812B, LED_SMD:LED_WS2812B_PLCC4_5.0x5.0mm_P3.2mm, F.Cu at (317.0, 159.5)
- added D163: WS2812B, LED_SMD:LED_WS2812B_PLCC4_5.0x5.0mm_P3.2mm, F.Cu at (326.5, 159.5)
- added D164: WS2812B, LED_SMD:LED_WS2812B_PLCC4_5.0x5.0mm_P3.2mm, F.Cu at (338.5, 159.5)
- added D165: WS2812B, LED_SMD:LED_WS2812B_PLCC4_5.0x5.0mm_P3.2mm, F.Cu at (176.0, 181.0)
- added D166: WS2812B, LED_SMD:LED_WS2812B_PLCC4_5.0x5.0mm_P3.2mm, F.Cu at (188.0, 181.0)
- added D167: WS2812B, LED_SMD:LED_WS2812B_PLCC4_5.0x5.0mm_P3.2mm, F.Cu at (197.5, 181.0)
- added D168: WS2812B, LED_SMD:LED_WS2812B_PLCC4_5.0x5.0mm_P3.2mm, F.Cu at (209.5, 181.0)
- added D169: WS2812B, LED_SMD:LED_WS2812B_PLCC4_5.0x5.0mm_P3.2mm, F.Cu at (219.0, 181.0)
- added D170: WS2812B, LED_SMD:LED_WS2812B_PLCC4_5.0x5.0mm_P3.2mm, F.Cu at (231.0, 181.0)
- added D171: WS2812B, LED_SMD:LED_WS2812B_PLCC4_5.0x5.0mm_P3.2mm, F.Cu at (240.5, 181.0)
- added D172: WS2812B, LED_SMD:LED_WS2812B_PLCC4_5.0x5.0mm_P3.2mm, F.Cu at (252.5, 181.0)
- added D173: WS2812B, LED_SMD:LED_WS2812B_PLCC4_5.0x5.0mm_P3.2mm, F.Cu at (262.0, 181.0)
- added D174: WS2812B, LED_SMD:LED_WS2812B_PLCC4_5.0x5.0mm_P3.2mm, F.Cu at (274.0, 181.0)
- added D175: WS2812B, LED_SMD:LED_WS2812B_PLCC4_5.0x5.0mm_P3.2mm, F.Cu at (283.5, 181.0)
- added D176: WS2812B, LED_SMD:LED_WS2812B_PLCC4_5.0x5.0mm_P3.2mm, F.Cu at (295.5, 181.0)
- added D177: WS2812B, LED_SMD:LED_WS2812B_PLCC4_5.0x5.0mm_P3.2mm, F.Cu at (305.0, 181.0)
- added D178: WS2812B, LED_SMD:LED_WS2812B_PLCC4_5.0x5.0mm_P3.2mm, F.Cu at (317.0, 181.0)
- added D179: WS2812B, LED_SMD:LED_WS2812B_PLCC4_5.0x5.0mm_P3.2mm, F.Cu at (326.5, 181.0)
- added D180: WS2812B, LED_SMD:LED_WS2812B_PLCC4_5.0x5.0mm_P3.2mm, F.Cu at (338.5, 181.0)
- added D181: WS2812B, LED_SMD:LED_WS2812B_PLCC4_5.0x5.0mm_P3.2mm, F.Cu at (176.0, 202.5)
- added D182: WS2812B, LED_SMD:LED_WS2812B_PLCC4_5.0x5.0mm_P3.2mm, F.Cu at (188.0, 202.5)
- added D183: WS2812B, LED_SMD:LED_WS2812B_PLCC4_5.0x5.0mm_P3.2mm, F.Cu at (197.5, 202.5)
- added D184: WS2812B, LED_SMD:LED_WS2812B_PLCC4_5.0x5.0mm_P3.2mm, F.Cu at (209.5, 202.5)
- added D185: WS2812B, LED_SMD:LED_WS2812B_PLCC4_5.0x5.0mm_P3.2mm, F.Cu at (219.0, 202.5)
- added D186: WS2812B, LED_SMD:LED_WS2812B_PLCC4_5.0x5.0mm_P3.2mm, F.Cu at (231.0, 202.5)
- added D187: WS2812B, LED_SMD:LED_WS2812B_PLCC4_5.0x5.0mm_P3.2mm, F.Cu at (240.5, 202.5)
- added D188: WS2812B, LED_SMD:LED_WS2812B_PLCC4_5.0x5.0mm_P3.2mm, F.Cu at (252.5, 202.5)
- added D189: WS2812B, LED_SMD:LED_WS2812B_PLCC4_5.0x5.0mm_P3.2mm, F.Cu at (262.0, 202.5)
- added D190: WS2812B, LED_SMD:LED_WS2812B_PLCC4_5.0x5.0mm_P3.2mm, F.Cu at (274.0, 202.5)
- added D191: WS2812B, LED_SMD:LED_WS2812B_PLCC4_5.0x5.0mm_P3.2mm, F.Cu at (283.5, 202.5)
- added D192: WS2812B, LED_SMD:LED_WS2812B_PLCC4_5.0x5.0mm_P3.2mm, F.Cu at (295.5, 202.5)
- added D193: WS2812B, LED_SMD:LED_WS2812B_PLCC4_5.0x5.0mm_P3.2mm, F.Cu at (305.0, 202.5)
- added D194: WS2812B, LED_SMD:LED_WS2812B_PLCC4_5.0x5.0mm_P3.2mm, F.Cu at (317.0, 202.5)
- added D195: WS2812B, LED_SMD:LED_WS2812B_PLCC4_5.0x5.0mm_P3.2mm, F.Cu at (326.5, 202.5)
- added D196: WS2812B, LED_SMD:LED_WS2812B_PLCC4_5.0x5.0mm_P3.2mm, F.Cu at (338.5, 202.5)
- added D197: WS2812B, LED_SMD:LED_WS2812B_PLCC4_5.0x5.0mm_P3.2mm, F.Cu at (176.0, 224.0)
- added D198: WS2812B, LED_SMD:LED_WS2812B_PLCC4_5.0x5.0mm_P3.2mm, F.Cu at (188.0, 224.0)
- added D199: WS2812B, LED_SMD:LED_WS2812B_PLCC4_5.0x5.0mm_P3.2mm, F.Cu at (197.5, 224.0)
- added D200: WS2812B, LED_SMD:LED_WS2812B_PLCC4_5.0x5.0mm_P3.2mm, F.Cu at (209.5, 224.0)
- added D201: WS2812B, LED_SMD:LED_WS2812B_PLCC4_5.0x5.0mm_P3.2mm, F.Cu at (219.0, 224.0)
- added D202: WS2812B, LED_SMD:LED_WS2812B_PLCC4_5.0x5.0mm_P3.2mm, F.Cu at (231.0, 224.0)
- added D203: WS2812B, LED_SMD:LED_WS2812B_PLCC4_5.0x5.0mm_P3.2mm, F.Cu at (240.5, 224.0)
- added D204: WS2812B, LED_SMD:LED_WS2812B_PLCC4_5.0x5.0mm_P3.2mm, F.Cu at (252.5, 224.0)
- added D205: WS2812B, LED_SMD:LED_WS2812B_PLCC4_5.0x5.0mm_P3.2mm, F.Cu at (262.0, 224.0)
- added D206: WS2812B, LED_SMD:LED_WS2812B_PLCC4_5.0x5.0mm_P3.2mm, F.Cu at (274.0, 224.0)
- added D207: WS2812B, LED_SMD:LED_WS2812B_PLCC4_5.0x5.0mm_P3.2mm, F.Cu at (283.5, 224.0)
- added D208: WS2812B, LED_SMD:LED_WS2812B_PLCC4_5.0x5.0mm_P3.2mm, F.Cu at (295.5, 224.0)
- added D209: WS2812B, LED_SMD:LED_WS2812B_PLCC4_5.0x5.0mm_P3.2mm, F.Cu at (305.0, 224.0)
- added D210: WS2812B, LED_SMD:LED_WS2812B_PLCC4_5.0x5.0mm_P3.2mm, F.Cu at (317.0, 224.0)
- added D211: WS2812B, LED_SMD:LED_WS2812B_PLCC4_5.0x5.0mm_P3.2mm, F.Cu at (326.5, 224.0)
- added D212: WS2812B, LED_SMD:LED_WS2812B_PLCC4_5.0x5.0mm_P3.2mm, F.Cu at (338.5, 224.0)
- added D213: WS2812B, LED_SMD:LED_WS2812B_PLCC4_5.0x5.0mm_P3.2mm, F.Cu at (176.0, 245.5)
- added D214: WS2812B, LED_SMD:LED_WS2812B_PLCC4_5.0x5.0mm_P3.2mm, F.Cu at (188.0, 245.5)
- added D215: WS2812B, LED_SMD:LED_WS2812B_PLCC4_5.0x5.0mm_P3.2mm, F.Cu at (197.5, 245.5)
- added D216: WS2812B, LED_SMD:LED_WS2812B_PLCC4_5.0x5.0mm_P3.2mm, F.Cu at (209.5, 245.5)
- added D217: WS2812B, LED_SMD:LED_WS2812B_PLCC4_5.0x5.0mm_P3.2mm, F.Cu at (219.0, 245.5)
- added D218: WS2812B, LED_SMD:LED_WS2812B_PLCC4_5.0x5.0mm_P3.2mm, F.Cu at (231.0, 245.5)
- added D219: WS2812B, LED_SMD:LED_WS2812B_PLCC4_5.0x5.0mm_P3.2mm, F.Cu at (240.5, 245.5)
- added D220: WS2812B, LED_SMD:LED_WS2812B_PLCC4_5.0x5.0mm_P3.2mm, F.Cu at (252.5, 245.5)
- added D221: WS2812B, LED_SMD:LED_WS2812B_PLCC4_5.0x5.0mm_P3.2mm, F.Cu at (262.0, 245.5)
- added D222: WS2812B, LED_SMD:LED_WS2812B_PLCC4_5.0x5.0mm_P3.2mm, F.Cu at (274.0, 245.5)
- added D223: WS2812B, LED_SMD:LED_WS2812B_PLCC4_5.0x5.0mm_P3.2mm, F.Cu at (283.5, 245.5)
- added D224: WS2812B, LED_SMD:LED_WS2812B_PLCC4_5.0x5.0mm_P3.2mm, F.Cu at (295.5, 245.5)
- added D225: WS2812B, LED_SMD:LED_WS2812B_PLCC4_5.0x5.0mm_P3.2mm, F.Cu at (305.0, 245.5)
- added D226: WS2812B, LED_SMD:LED_WS2812B_PLCC4_5.0x5.0mm_P3.2mm, F.Cu at (317.0, 245.5)
- added D227: WS2812B, LED_SMD:LED_WS2812B_PLCC4_5.0x5.0mm_P3.2mm, F.Cu at (326.5, 245.5)
- added D228: WS2812B, LED_SMD:LED_WS2812B_PLCC4_5.0x5.0mm_P3.2mm, F.Cu at (338.5, 245.5)
- added D229: WS2812B, LED_SMD:LED_WS2812B_PLCC4_5.0x5.0mm_P3.2mm, F.Cu at (184.0, 50.6)
- added D230: WS2812B, LED_SMD:LED_WS2812B_PLCC4_5.0x5.0mm_P3.2mm, F.Cu at (199.0, 50.6)
- added D231: WS2812B, LED_SMD:LED_WS2812B_PLCC4_5.0x5.0mm_P3.2mm, F.Cu at (214.0, 50.6)
- added D232: WS2812B, LED_SMD:LED_WS2812B_PLCC4_5.0x5.0mm_P3.2mm, F.Cu at (229.0, 50.6)
- added D233: WS2812B, LED_SMD:LED_WS2812B_PLCC4_5.0x5.0mm_P3.2mm, F.Cu at (184.0, 67.6)
- added D234: WS2812B, LED_SMD:LED_WS2812B_PLCC4_5.0x5.0mm_P3.2mm, F.Cu at (199.0, 67.6)
- added D235: WS2812B, LED_SMD:LED_WS2812B_PLCC4_5.0x5.0mm_P3.2mm, F.Cu at (214.0, 67.6)
- added D236: WS2812B, LED_SMD:LED_WS2812B_PLCC4_5.0x5.0mm_P3.2mm, F.Cu at (229.0, 67.6)
- R24, R25, R26, R27, R28, R29, R30, R31, R32, R33, R34, R35, R36, R37, R38, R39, R40, R41, R42, R43, R44, R45, R46, R47: footprint Potentiometer_THT:Potentiometer_Alps_RK09L_Single_Vertical -> ordentliche-teile:Potentiometer_vom_markt
- moved U45 8.50 mm to (253.0, 87.5)
- moved U74 6.96 mm to (325.0, 131.0)
- moved U64 6.80 mm to (325.0, 110.0)
- moved U69 6.58 mm to (239.0, 132.0)
- moved U56 6.23 mm to (195.5, 110.0)
- moved U113 5.70 mm to (322.6, 216.8)
- moved U50 5.24 mm to (261.5, 87.5)
- moved U103 5.05 mm to (322.1, 195.3)
- moved U53 4.84 mm to (295.9, 88.0)
- moved U88 4.80 mm to (235.6, 173.8)
- moved U80 4.61 mm to (279.0, 152.0)
- moved U105 4.15 mm to (192.6, 217.3)
- moved U90 3.94 mm to (278.6, 174.8)
- moved U110 3.91 mm to (278.6, 217.8)
- moved U57 3.81 mm to (219.0, 109.0)
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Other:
- board size 172 x 392.2 mm -> 172.5 x 392 mm
